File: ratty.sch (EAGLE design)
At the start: 89 parts, among them IC2 L293DD, Q1 BS170, Q2 BS170, Q3 BS170, Q5 BS170, U1 ITG-32001:1

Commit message: More routing, more naming
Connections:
- net N$11 renamed LED/R11
- net N$6 renamed LED/R5
- net N$8 renamed LED/R7
- net N$9 renamed LED/R14
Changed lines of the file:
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@@
 </segment>
 </net>
-<net name="N$6" class="0">
+<net name="LED/R5" class="0">
 <segment>
 <pinref part="U$15" gate="G$1" pin="-"/>
@@
 </segment>
 </net>
-<net name="N$8" class="0">
+<net name="LED/R7" class="0">
 <segment>
 <pinref part="U$16" gate="G$1" pin="-"/>
@@
 </segment>
 </net>
-<net name="N$11" class="0">
+<net name="LED/R11" class="0">
 <segment>
 <pinref part="U$18" gate="G$1" pin="-"/>
@@
 </segment>
 </net>
-<net name="N$9" class="0">
+<net name="LED/R14" class="0">
 <segment>
 <pinref part="U$19" gate="G$1" pin="-"/>

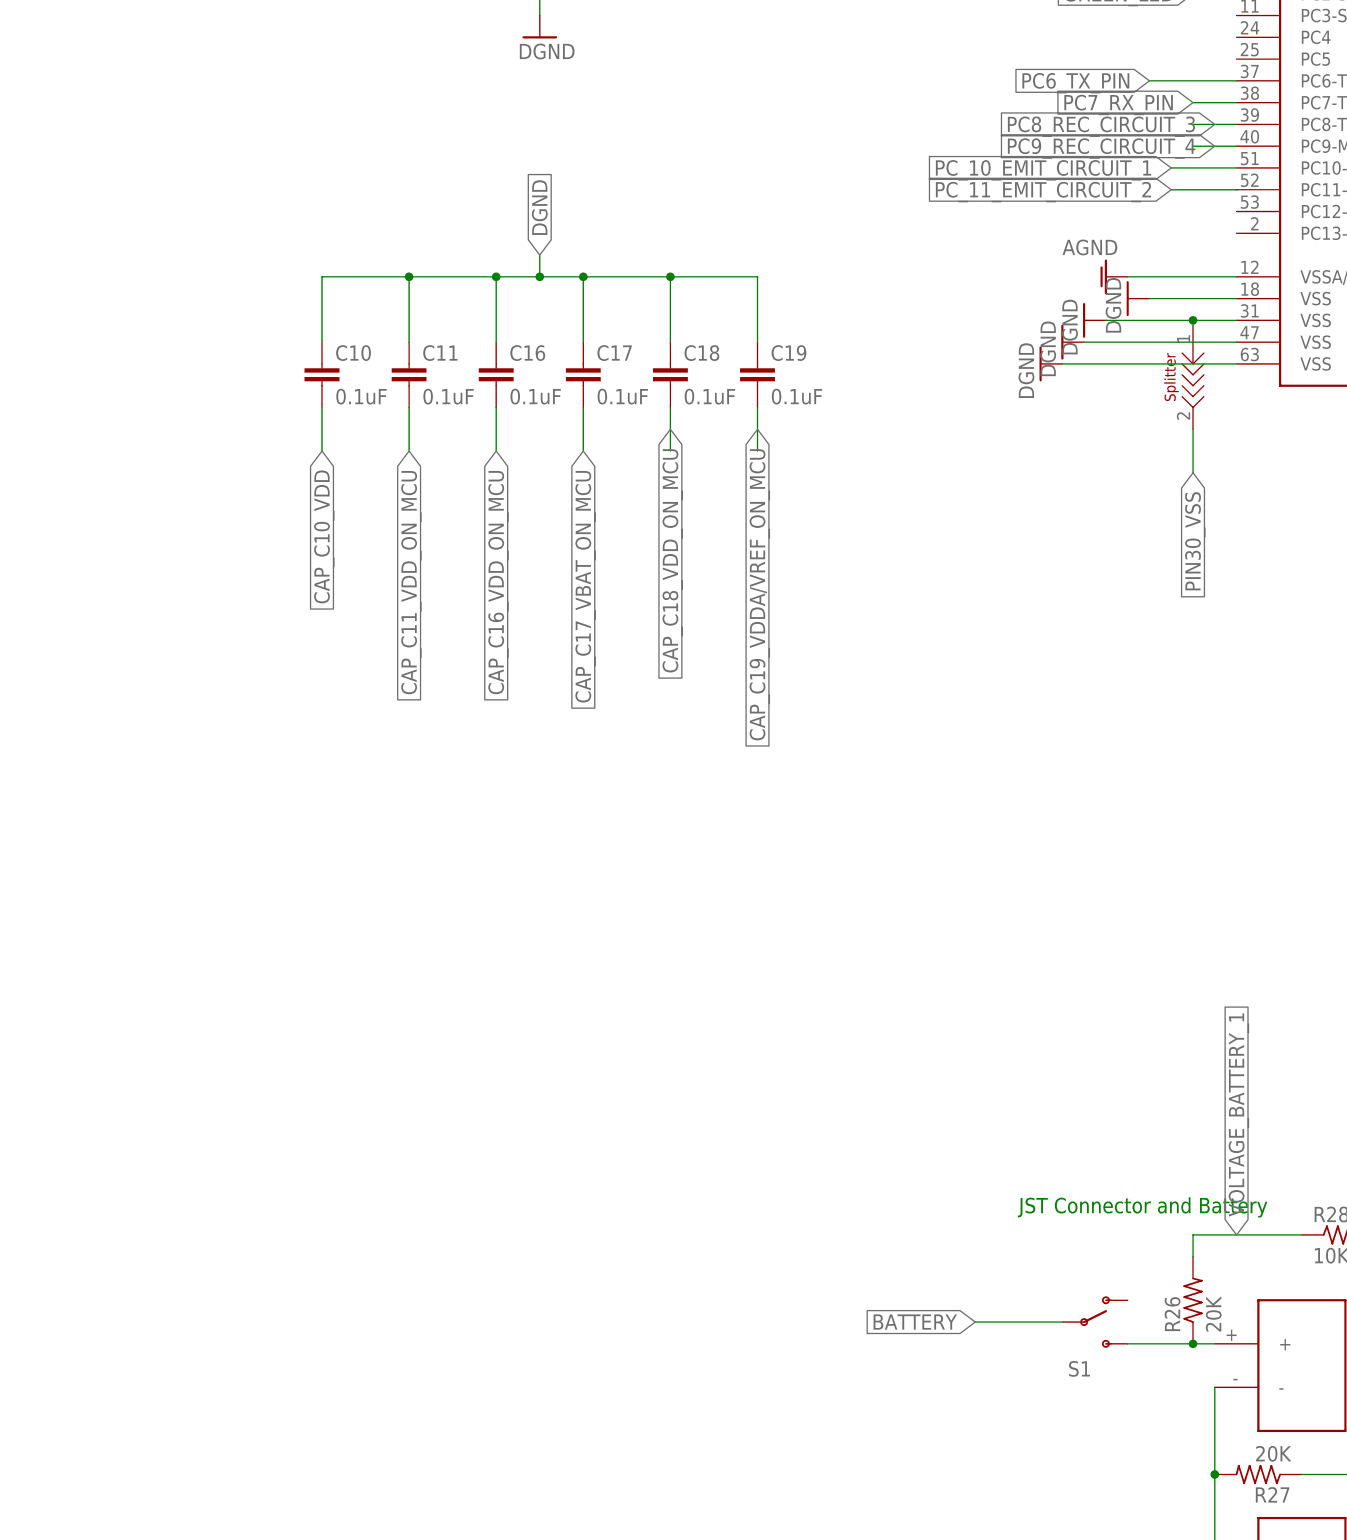
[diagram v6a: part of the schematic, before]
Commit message: Need to change capacitors, changed the switch
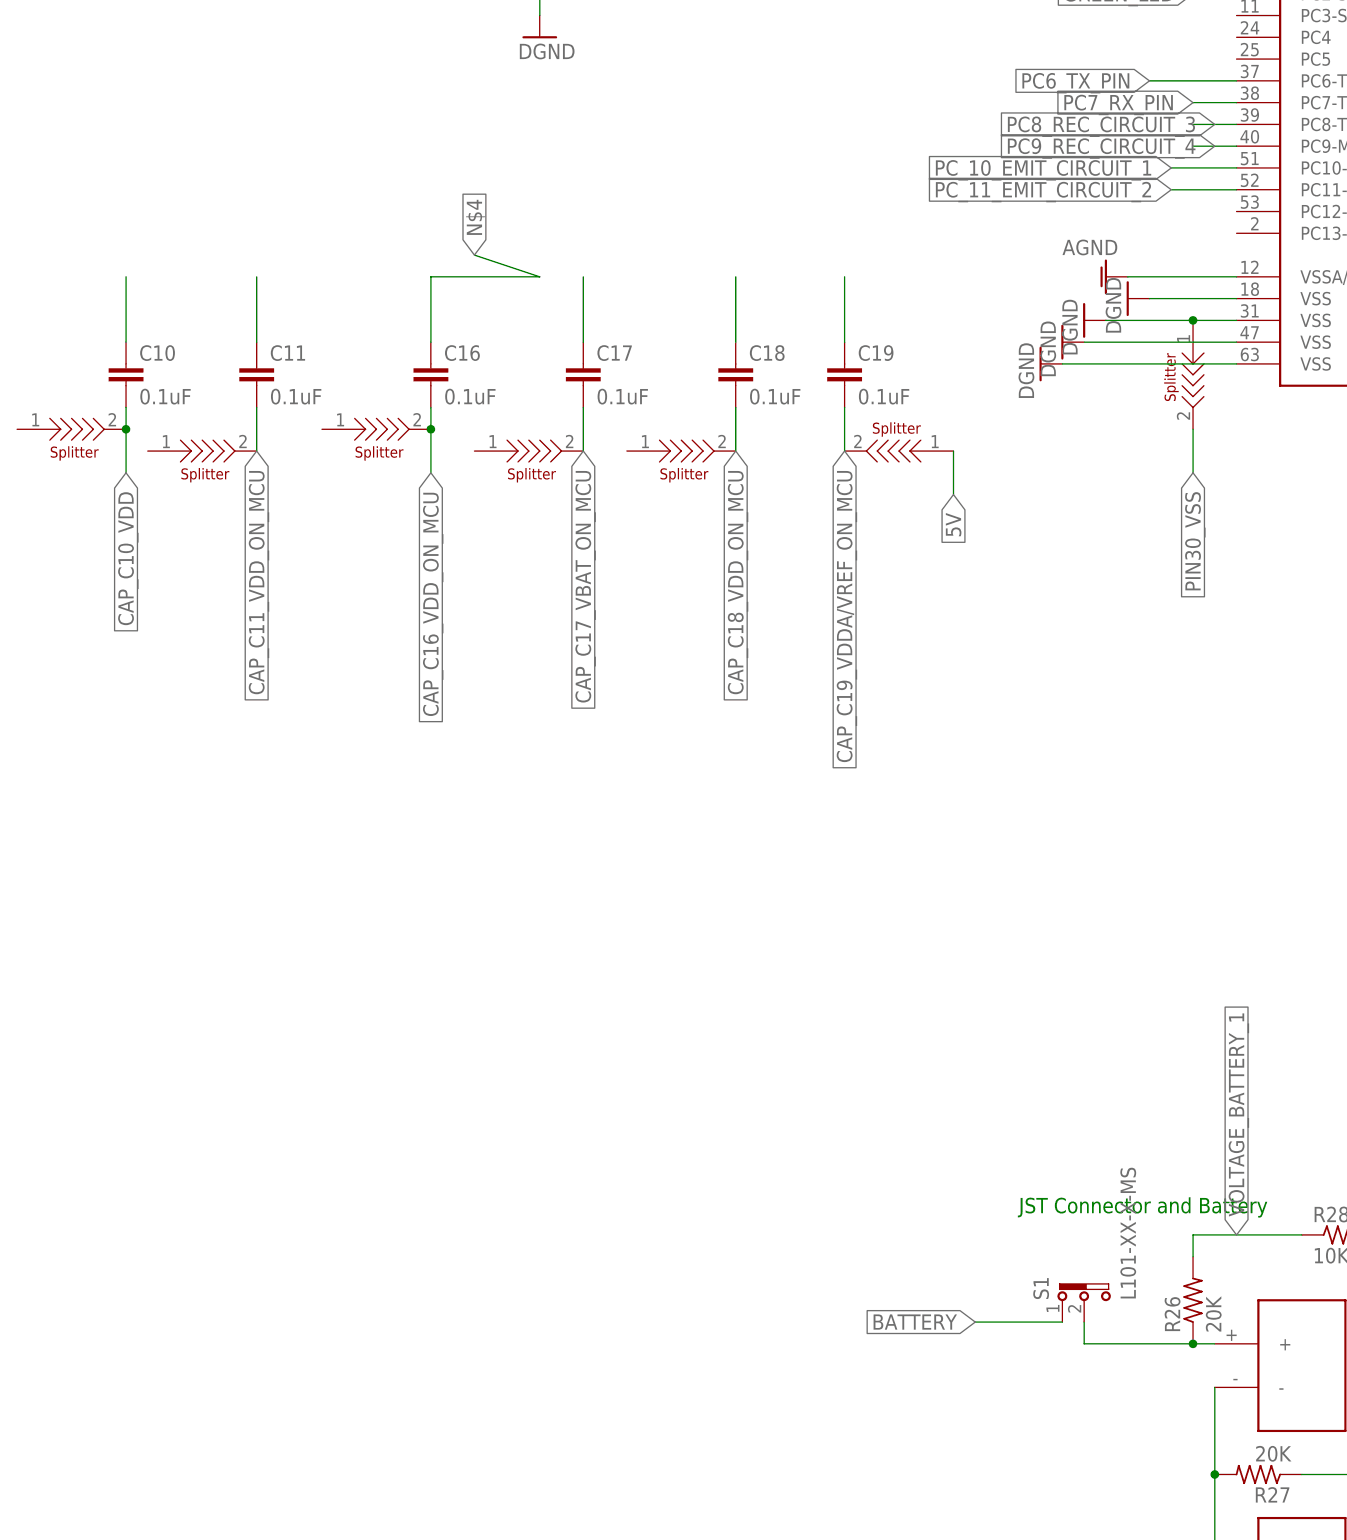
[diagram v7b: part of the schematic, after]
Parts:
- added U$10, U$12, U$14, U$20, U$21, U$7: SPLITTER, splitter:SPLITTER
- S1: value (none) -> L101-XX-X-MS; device SparkFun-Electromechanical:SWITCH-SPDTPTH -> switch-ck:L101-XX-X-MS
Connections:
- new net N$1: C10.1
- new net N$3: C11.1
- new net N$4: C16.1
- new net N$5: C17.1
- new net N$6: C18.1
- net 5V: now also U$21.1
- net BATTERY: now also S1.1; no longer S1.P
- net BATTERY_1: now also S1.2; no longer S1.S
- net CAP_C10_VDD: now also U$7.2
- net CAP_C11_VDD_ON_MCU: now also U$10.2
- net CAP_C16_VDD_ON_MCU: now also U$12.2
- net CAP_C17_VBAT_ON_MCU: now also U$14.2
- net CAP_C18_VDD_ON_MCU: now also U$20.2
- net CAP_C19_VDDA/VREF_ON_MCU: now also U$21.2
- net DGND: no longer C10.1, C11.1, C16.1, C17.1, C18.1
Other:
- moved on the sheet: C10, C11, C16, C18, C19
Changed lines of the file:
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@@
 <part name="U$1" library="JST_CONNECTOR_FEMALE. through hole" deviceset="JST_CONNECTOR_FEMALE" device=""/>
 <part name="U$2" library="JST_CONNECTOR_FEMALE. through hole" deviceset="JST_CONNECTOR_FEMALE" device=""/>
-<part name="S1" library="SparkFun-Electromechanical" deviceset="SWITCH-SPDT" device="PTH"/>
 <part name="U$3" library="TPS76850(SOIC-8)" deviceset="TPS76850(SOIC-8)" device=""/>
 <part name="GND2" library="SparkFun" deviceset="GND" device=""/>
@@
 <part name="AGND8" library="supply1" deviceset="AGND" device=""/>
 <part name="GND27" library="SparkFun-Aesthetics" deviceset="DGND" device=""/>
+<part name="S1" library="switch-ck" deviceset="L101-XX-X-MS" device=""/>
+<part name="U$7" library="splitter" deviceset="SPLITTER" device=""/>
+<part name="U$10" library="splitter" deviceset="SPLITTER" device=""/>
+<part name="U$12" library="splitter" deviceset="SPLITTER" device=""/>
+<part name="U$14" library="splitter" deviceset="SPLITTER" device=""/>
+<part name="U$20" library="splitter" deviceset="SPLITTER" device=""/>
+<part name="U$21" library="splitter" deviceset="SPLITTER" device=""/>
 </parts>
 <sheets>
@@
 <instance part="U$1" gate="G$1" x="68.58" y="106.68" rot="R270"/>
 <instance part="U$2" gate="G$1" x="68.58" y="81.28" rot="R270"/>
-<instance part="S1" gate="1" x="43.18" y="111.76"/>
 <instance part="U$3" gate="G$1" x="129.54" y="144.78"/>
 <instance part="GND2" gate="1" x="109.22" y="91.44"/>
@@
 <instance part="IC2" gate="G$1" x="233.68" y="35.56"/>
 <instance part="U$4" gate="G$1" x="132.08" y="276.86"/>
-<instance part="C10" gate="G$1" x="-45.72" y="223.52"/>
-<instance part="C11" gate="G$1" x="-35.56" y="223.52"/>
-<instance part="C16" gate="G$1" x="-25.4" y="223.52"/>
+<instance part="C10" gate="G$1" x="-68.58" y="223.52"/>
+<instance part="C11" gate="G$1" x="-53.34" y="223.52"/>
+<instance part="C16" gate="G$1" x="-33.02" y="223.52"/>
 <instance part="C17" gate="G$1" x="-15.24" y="223.52"/>
-<instance part="C18" gate="G$1" x="-5.08" y="223.52"/>
-<instance part="C19" gate="G$1" x="5.08" y="223.52"/>
+<instance part="C18" gate="G$1" x="2.54" y="223.52"/>
+<instance part="C19" gate="G$1" x="15.24" y="223.52"/>
 <instance part="R2" gate="G$1" x="5.08" y="294.64"/>
 <instance part="RESETBUTTON" gate="G$1" x="-20.32" y="281.94" rot="R180"/>
@@
 <instance part="AGND8" gate="VR1" x="99.06" y="93.98" rot="R90"/>
 <instance part="GND27" gate="G$1" x="213.36" y="236.22" rot="R90"/>
+<instance part="S1" gate="G$1" x="43.18" y="114.3" rot="R90"/>
+<instance part="U$7" gate="G$1" x="-73.66" y="215.9"/>
+<instance part="U$10" gate="G$1" x="-58.42" y="213.36"/>
+<instance part="U$12" gate="G$1" x="-38.1" y="215.9"/>
+<instance part="U$14" gate="G$1" x="-20.32" y="213.36"/>
+<instance part="U$20" gate="G$1" x="-2.54" y="213.36"/>
+<instance part="U$21" gate="G$1" x="20.32" y="213.36" rot="R180"/>
 </instances>
 <busses>
@@
 <label x="375.92" y="-15.24" size="1.778" layer="95" rot="R270" xref="yes"/>
 </segment>
+<segment>
+<pinref part="U$21" gate="G$1" pin="1"/>
+<wire x1="27.94" y1="213.36" x2="27.94" y2="208.28" width="0.1524" layer="91"/>
+<label x="27.94" y="208.28" size="1.778" layer="95" rot="R270" xref="yes"/>
+</segment>
 </net>
 <net name="BATTERY_1" class="0">
 <segment>
 <pinref part="U$1" gate="G$1" pin="+"/>
-<pinref part="S1" gate="1" pin="S"/>
-<wire x1="48.26" y1="109.22" x2="55.88" y2="109.22" width="0.1524" layer="91"/>
+<wire x1="43.18" y1="109.22" x2="55.88" y2="109.22" width="0.1524" layer="91"/>
 <pinref part="R26" gate="G$1" pin="1"/>
 <wire x1="55.88" y1="109.22" x2="58.42" y2="109.22" width="0.1524" layer="91"/>
 <junction x="55.88" y="109.22"/>
+<pinref part="S1" gate="G$1" pin="2"/>
+<wire x1="43.18" y1="111.76" x2="43.18" y2="109.22" width="0.1524" layer="91"/>
 </segment>
 </net>
 <net name="BATTERY" class="0">
 <segment>
-<pinref part="S1" gate="1" pin="P"/>
 <wire x1="30.48" y1="111.76" x2="40.64" y2="111.76" width="0.1524" layer="91"/>
 <label x="30.48" y="111.76" size="1.778" layer="95" rot="R180" xref="yes"/>
+<pinref part="S1" gate="G$1" pin="1"/>
 </segment>
 <segment>
@@
 <wire x1="-15.24" y1="218.44" x2="-15.24" y2="213.36" width="0.1524" layer="91"/>
 <label x="-15.24" y="213.36" size="1.778" layer="95" rot="R270" xref="yes"/>
+<pinref part="U$14" gate="G$1" pin="2"/>
 </segment>
 <segment>
@@
 <segment>
 <pinref part="C10" gate="G$1" pin="2"/>
-<wire x1="-45.72" y1="218.44" x2="-45.72" y2="213.36" width="0.1524" layer="91"/>
-<label x="-45.72" y="213.36" size="1.778" layer="95" rot="R270" xref="yes"/>
+<wire x1="-68.58" y1="218.44" x2="-68.58" y2="215.9" width="0.1524" layer="91"/>
+<label x="-68.58" y="210.82" size="1.778" layer="95" rot="R270" xref="yes"/>
+<pinref part="U$7" gate="G$1" pin="2"/>
+<wire x1="-68.58" y1="215.9" x2="-68.58" y2="210.82" width="0.1524" layer="91"/>
+<junction x="-68.58" y="215.9"/>
 </segment>
 </net>
@@
 <segment>
 <pinref part="C11" gate="G$1" pin="2"/>
-<wire x1="-35.56" y1="218.44" x2="-35.56" y2="213.36" width="0.1524" layer="91"/>
-<label x="-35.56" y="213.36" size="1.778" layer="95" rot="R270" xref="yes"/>
+<wire x1="-53.34" y1="218.44" x2="-53.34" y2="213.36" width="0.1524" layer="91"/>
+<label x="-53.34" y="213.36" size="1.778" layer="95" rot="R270" xref="yes"/>
+<pinref part="U$10" gate="G$1" pin="2"/>
 </segment>
 </net>
@@
 <segment>
 <pinref part="C16" gate="G$1" pin="2"/>
-<wire x1="-25.4" y1="218.44" x2="-25.4" y2="213.36" width="0.1524" layer="91"/>
-<label x="-25.4" y="213.36" size="1.778" layer="95" rot="R270" xref="yes"/>
+<wire x1="-33.02" y1="218.44" x2="-33.02" y2="215.9" width="0.1524" layer="91"/>
+<label x="-33.02" y="210.82" size="1.778" layer="95" rot="R270" xref="yes"/>
+<pinref part="U$12" gate="G$1" pin="2"/>
+<wire x1="-33.02" y1="215.9" x2="-33.02" y2="210.82" width="0.1524" layer="91"/>
+<junction x="-33.02" y="215.9"/>
 </segment>
 </net>
@@
 <segment>
 <pinref part="C18" gate="G$1" pin="2"/>
-<wire x1="-5.08" y1="218.44" x2="-5.08" y2="213.36" width="0.1524" layer="91"/>
-<label x="-5.08" y="215.9" size="1.778" layer="95" rot="R270" xref="yes"/>
+<wire x1="2.54" y1="218.44" x2="2.54" y2="213.36" width="0.1524" layer="91"/>
+<label x="2.54" y="213.36" size="1.778" layer="95" rot="R270" xref="yes"/>
+<pinref part="U$20" gate="G$1" pin="2"/>
 </segment>
 </net>
@@
 <segment>
 <pinref part="C19" gate="G$1" pin="2"/>
-<wire x1="5.08" y1="218.44" x2="5.08" y2="213.36" width="0.1524" layer="91"/>
-<label x="5.08" y="215.9" size="1.778" layer="95" rot="R270" xref="yes"/>
+<wire x1="15.24" y1="218.44" x2="15.24" y2="213.36" width="0.1524" layer="91"/>
+<label x="15.24" y="213.36" size="1.778" layer="95" rot="R270" xref="yes"/>
+<pinref part="U$21" gate="G$1" pin="2"/>
 </segment>
 </net>
@@
 </segment>
 <segment>
-<pinref part="C10" gate="G$1" pin="1"/>
-<wire x1="-45.72" y1="226.06" x2="-45.72" y2="233.68" width="0.1524" layer="91"/>
-<pinref part="C11" gate="G$1" pin="1"/>
-<wire x1="-45.72" y1="233.68" x2="-35.56" y2="233.68" width="0.1524" layer="91"/>
-<wire x1="-35.56" y1="233.68" x2="-35.56" y2="226.06" width="0.1524" layer="91"/>
-<wire x1="-35.56" y1="233.68" x2="-25.4" y2="233.68" width="0.1524" layer="91"/>
-<junction x="-35.56" y="233.68"/>
-<pinref part="C16" gate="G$1" pin="1"/>
-<wire x1="-25.4" y1="233.68" x2="-25.4" y2="226.06" width="0.1524" layer="91"/>
-<pinref part="C17" gate="G$1" pin="1"/>
-<wire x1="-25.4" y1="233.68" x2="-20.32" y2="233.68" width="0.1524" layer="91"/>
-<wire x1="-20.32" y1="233.68" x2="-15.24" y2="233.68" width="0.1524" layer="91"/>
-<wire x1="-15.24" y1="233.68" x2="-15.24" y2="226.06" width="0.1524" layer="91"/>
-<junction x="-25.4" y="233.68"/>
-<pinref part="C18" gate="G$1" pin="1"/>
-<wire x1="-15.24" y1="233.68" x2="-5.08" y2="233.68" width="0.1524" layer="91"/>
-<wire x1="-5.08" y1="233.68" x2="-5.08" y2="226.06" width="0.1524" layer="91"/>
-<junction x="-15.24" y="233.68"/>
 <pinref part="C19" gate="G$1" pin="1"/>
-<wire x1="-5.08" y1="233.68" x2="5.08" y2="233.68" width="0.1524" layer="91"/>
-<wire x1="5.08" y1="233.68" x2="5.08" y2="226.06" width="0.1524" layer="91"/>
-<junction x="-5.08" y="233.68"/>
-<wire x1="-20.32" y1="233.68" x2="-20.32" y2="236.22" width="0.1524" layer="91"/>
-<junction x="-20.32" y="233.68"/>
-<label x="-20.32" y="236.22" size="1.778" layer="95" rot="R90" xref="yes"/>
+<wire x1="15.24" y1="233.68" x2="15.24" y2="226.06" width="0.1524" layer="91"/>
 </segment>
 <segment>
@@
 </segment>
 </net>
+<net name="N$1" class="0">
+<segment>
+<pinref part="C10" gate="G$1" pin="1"/>
+<wire x1="-68.58" y1="226.06" x2="-68.58" y2="233.68" width="0.1524" layer="91"/>
+</segment>
+</net>
+<net name="N$3" class="0">
+<segment>
+<pinref part="C11" gate="G$1" pin="1"/>
+<wire x1="-53.34" y1="233.68" x2="-53.34" y2="226.06" width="0.1524" layer="91"/>
+</segment>
+</net>
+<net name="N$4" class="0">
+<segment>
+<pinref part="C16" gate="G$1" pin="1"/>
+<wire x1="-20.32" y1="233.68" x2="-27.94" y2="236.22" width="0.1524" layer="91"/>
+<wire x1="-33.02" y1="233.68" x2="-20.32" y2="233.68" width="0.1524" layer="91"/>
+<wire x1="-33.02" y1="233.68" x2="-33.02" y2="226.06" width="0.1524" layer="91"/>
+<label x="-27.94" y="236.22" size="1.778" layer="95" rot="R90" xref="yes"/>
+</segment>
+</net>
+<net name="N$5" class="0">
+<segment>
+<pinref part="C17" gate="G$1" pin="1"/>
+<wire x1="-15.24" y1="233.68" x2="-15.24" y2="226.06" width="0.1524" layer="91"/>
+</segment>
+</net>
+<net name="N$6" class="0">
+<segment>
+<pinref part="C18" gate="G$1" pin="1"/>
+<wire x1="2.54" y1="233.68" x2="2.54" y2="226.06" width="0.1524" layer="91"/>
+</segment>
+</net>
